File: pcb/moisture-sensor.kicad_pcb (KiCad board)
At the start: 2 copper layers, 40 x 125 mm, 35 parts, among them J3 USB4110, U1 ESP32-C3-WROOM-02, U2 TPS631000, U4 MCP73832, Y1 32.768kHz

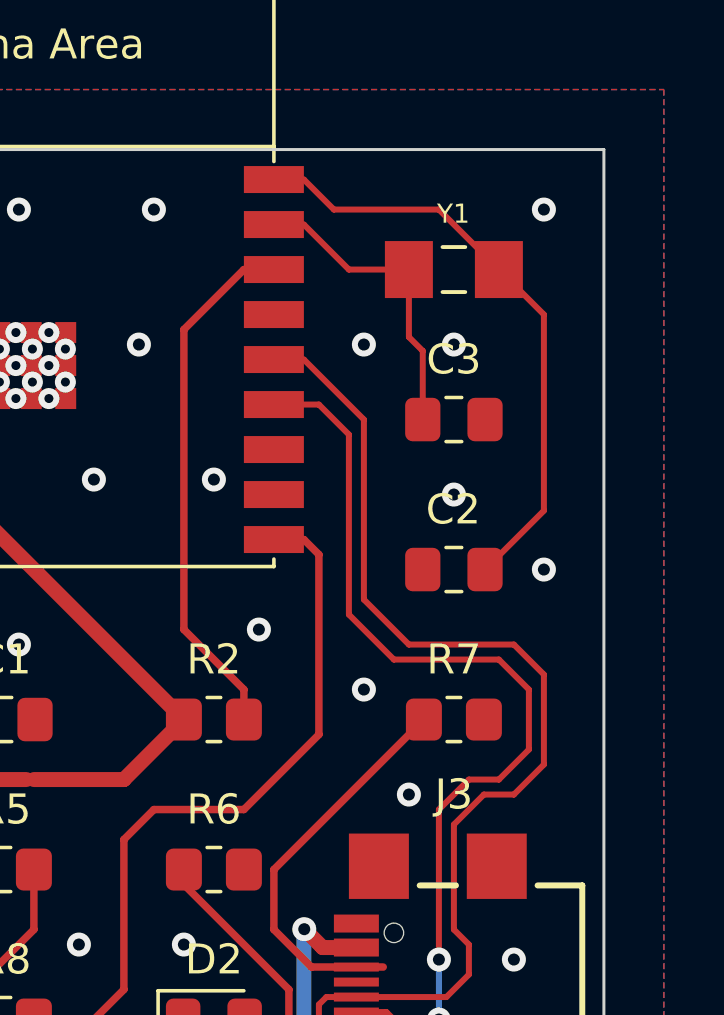
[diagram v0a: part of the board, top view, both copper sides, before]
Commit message: prefer built in KiCad items
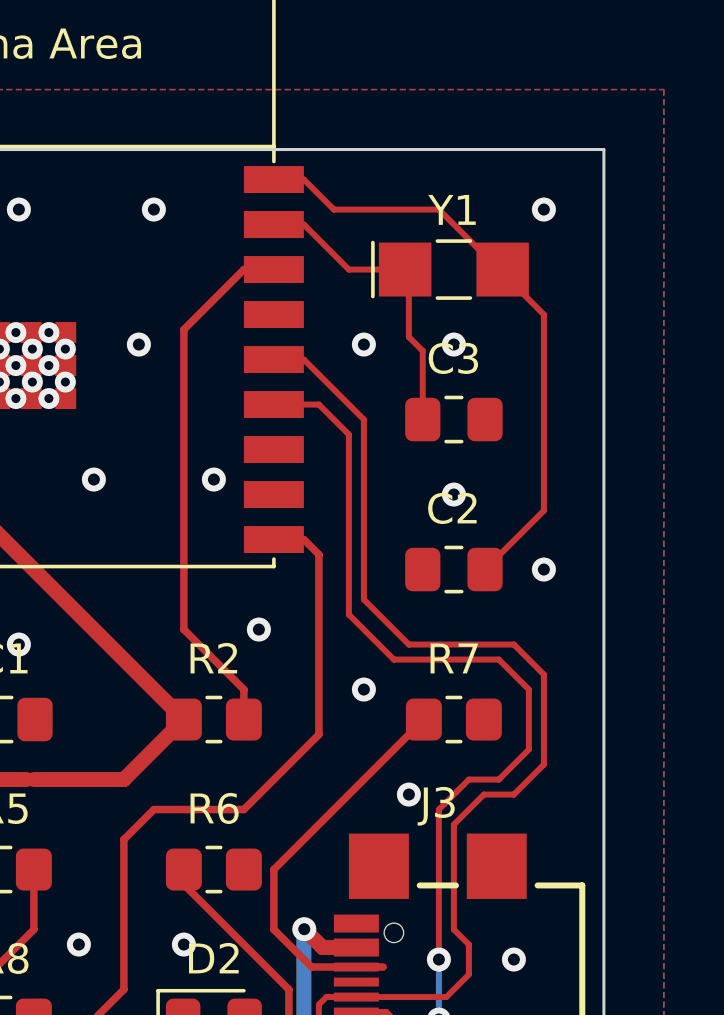
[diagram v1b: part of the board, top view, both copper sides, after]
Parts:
- J3: footprint library:GCT_USB4110-GF-A_REVB -> library:USB4110-GF-A_REVB
- Y1: footprint library:ABS07-32.768KHZ-T -> Crystal:Crystal_SMD_G8-2Pin_3.2x1.5mm_HandSoldering

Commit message: increase power supply capacitor sizes
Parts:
- C8, C9: value 10uF -> 47uF
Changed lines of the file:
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@@
     (descr "Capacitor SMD 0805 (2012 Metric), square (rectangular) end terminal, IPC_7351 nominal with elongated pad for handsoldering. (Body size source: IPC-SM-782 page 76, https://www.pcb-3d.com/wordpress/wp-content/uploads/ipc-sm-782a_amendment_1_and_2.pdf, https://docs.google.com/spreadsheets/d/1BsfQQcO9C6DZCsRaXUlFlo91Tg2WpOkGARC1WS5S8t0/edit?usp=sharing), generated with kicad-footprint-generator")
     (tags "capacitor handsolder")
-    (property "MPN" "GRM21BR71A106KA73")
+    (property "MPN" "GRM21BR61A476ME15")
     (property "Sheetfile" "moisture-sensor.kicad_sch")
     (property "Sheetname" "")
@@
       (effects (font (size 1 1) (thickness 0.15)))
     )
-    (fp_text value "10uF" (at 0 1.68) (layer "F.Fab")
+    (fp_text value "47uF" (at 0 1.68) (layer "F.Fab")
       (effects (font (size 1 1) (thickness 0.15)))
     )
@@
     (descr "Capacitor SMD 0805 (2012 Metric), square (rectangular) end terminal, IPC_7351 nominal with elongated pad for handsoldering. (Body size source: IPC-SM-782 page 76, https://www.pcb-3d.com/wordpress/wp-content/uploads/ipc-sm-782a_amendment_1_and_2.pdf, https://docs.google.com/spreadsheets/d/1BsfQQcO9C6DZCsRaXUlFlo91Tg2WpOkGARC1WS5S8t0/edit?usp=sharing), generated with kicad-footprint-generator")
     (tags "capacitor handsolder")
-    (property "MPN" "GRM21BR71A106KA73")
+    (property "MPN" "GRM21BR61A476ME15")
     (property "Sheetfile" "moisture-sensor.kicad_sch")
     (property "Sheetname" "")
@@
       (effects (font (size 1 1) (thickness 0.15)))
     )
-    (fp_text value "10uF" (at 0 1.68) (layer "F.Fab")
-      (effects (font (size 1 1) (thickness 0.15)))
-    )
+    (fp_text value "47uF" (at 0 1.68) (layer "F.Fab")
+      (effects (font (size 1 1) (thickness 0.15)))
+    )

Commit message: Revert "increase power supply capacitor sizes"
This reverts commit e628d20ff7827fca777ef456cf9c7b65b2cb21d5.
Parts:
- C8, C9: value 47uF -> 10uF
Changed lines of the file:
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@@
     (descr "Capacitor SMD 0805 (2012 Metric), square (rectangular) end terminal, IPC_7351 nominal with elongated pad for handsoldering. (Body size source: IPC-SM-782 page 76, https://www.pcb-3d.com/wordpress/wp-content/uploads/ipc-sm-782a_amendment_1_and_2.pdf, https://docs.google.com/spreadsheets/d/1BsfQQcO9C6DZCsRaXUlFlo91Tg2WpOkGARC1WS5S8t0/edit?usp=sharing), generated with kicad-footprint-generator")
     (tags "capacitor handsolder")
-    (property "MPN" "GRM21BR61A476ME15")
+    (property "MPN" "GRM21BR71A106KA73")
     (property "Sheetfile" "moisture-sensor.kicad_sch")
     (property "Sheetname" "")
@@
       (effects (font (size 1 1) (thickness 0.15)))
     )
-    (fp_text value "47uF" (at 0 1.68) (layer "F.Fab")
+    (fp_text value "10uF" (at 0 1.68) (layer "F.Fab")
       (effects (font (size 1 1) (thickness 0.15)))
     )
@@
     (descr "Capacitor SMD 0805 (2012 Metric), square (rectangular) end terminal, IPC_7351 nominal with elongated pad for handsoldering. (Body size source: IPC-SM-782 page 76, https://www.pcb-3d.com/wordpress/wp-content/uploads/ipc-sm-782a_amendment_1_and_2.pdf, https://docs.google.com/spreadsheets/d/1BsfQQcO9C6DZCsRaXUlFlo91Tg2WpOkGARC1WS5S8t0/edit?usp=sharing), generated with kicad-footprint-generator")
     (tags "capacitor handsolder")
-    (property "MPN" "GRM21BR61A476ME15")
+    (property "MPN" "GRM21BR71A106KA73")
     (property "Sheetfile" "moisture-sensor.kicad_sch")
     (property "Sheetname" "")
@@
       (effects (font (size 1 1) (thickness 0.15)))
     )
-    (fp_text value "47uF" (at 0 1.68) (layer "F.Fab")
-      (effects (font (size 1 1) (thickness 0.15)))
-    )
+    (fp_text value "10uF" (at 0 1.68) (layer "F.Fab")
+      (effects (font (size 1 1) (thickness 0.15)))
+    )
